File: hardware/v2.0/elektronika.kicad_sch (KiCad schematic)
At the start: 35 parts, among them J1 Conn_02x06_Odd_Even, J12 Conn_02x03_Counter_Clockwise, J2 Conn_01x06_Male, J3 Conn_01x06, Q4 Q_NMOS_GSD, Q5 Q_PMOS_GSD, Q6 Q_NMOS_GSD, Q7 Q_NMOS_GSD, Q8 Q_NMOS_GSD

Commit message: Secondary button cross
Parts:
- removed J12: Conn_02x03_Counter_Clockwise, Connector_PinSocket_2.54mm:PinSocket_2x03_P2.54mm_Vertical, symbol Connector_Generic:Conn_02x03_Counter_Clockwise
- added J12: Conn_01x02, Connector_PinSocket_2.54mm:PinSocket_1x02_P2.54mm_Vertical, symbol Connector_Generic:Conn_01x02
- added R32: 10k, Resistor_SMD:R_0402_1005Metric, symbol Device:R
- J1: footprint Connector_PinSocket_2.54mm:PinSocket_2x06_P2.54mm_Vertical -> Connector_PinSocket_2.54mm:PinSocket_2x06_P2.54mm_Horizontal
- J3: footprint Connector_PinSocket_2.54mm:PinSocket_1x06_P2.54mm_Vertical -> Connector_PinSocket_2.54mm:PinSocket_1x06_P2.54mm_Horizontal
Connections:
- net 3V3: now also R32.1; no longer Q7.1 (G), Q8.1 (G)
- net 5V: no longer R11.1, R18.1
- net ESP+programing/IO48: now also J12.1 (Pin_1)
- net GND: now also J12.2 (Pin_2)
- net IO15: now also J1.8 (Pin_8); no longer J1.2 (Pin_2)
- net IO16: now also J1.6 (Pin_6); no longer J1.4 (Pin_4)
- net IO17: now also J1.4 (Pin_4); no longer J1.6 (Pin_6)
- net IO18: now also J1.2 (Pin_2); no longer J1.8 (Pin_8)
- net IO35: now also J3.1 (Pin_1); no longer J1.1 (Pin_1)
- net IO36: now also J3.2 (Pin_2); no longer J1.3 (Pin_3)
- net IO37: now also J3.3 (Pin_3); no longer J1.5 (Pin_5)
- net IO38: now also J3.4 (Pin_4); no longer J1.7 (Pin_7)
- net IO39: now also J1.1 (Pin_1); no longer J3.1 (Pin_1)
- net IO40: now also J1.3 (Pin_3); no longer J3.2 (Pin_2)
- net IO41: now also J1.5 (Pin_5); no longer J3.3 (Pin_3)
- net IO42: now also J1.7 (Pin_7); no longer J3.4 (Pin_4)
- net SW_10: now also R10.2; no longer R12.2
- net SW_11: now also R9.2; no longer R14.2
- net SW_2: now also R6.2; no longer R1.2
- net SW_3: now also R7.2; no longer R4.2
- net SW_4: now also R12.2; no longer R6.2
- net SW_5: now also R4.2; no longer R7.2
- net SW_7: now also R1.2; no longer R8.2
- net SW_8: now also R8.2; no longer R9.2
- net SW_9: now also R14.2; no longer R10.2
- net VSTUP2: now also J2.4 (Pin_4); no longer J2.2 (Pin_2)
- net VSTUP3: now also J2.2 (Pin_2); no longer J2.4 (Pin_4)
- net V_LED_1: now also R11.1, R18.1
- new net EN: Q7.1 (G), Q8.1 (G)
- new net SW_12: R32.2
- no-connect marks 0 -> 1
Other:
- sheet ESP+programing ports: added EN; removed none

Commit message: SD karta and factory files
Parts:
- removed J2: Conn_01x06_Male, Connector_JST:JST_PH_S6B-PH-K_1x06_P2.00mm_Horizontal, symbol Connector:Conn_01x06_Male
- added C22, C23: 10uF, Capacitor_SMD:C_0603_1608Metric, symbol Device:C
- added J2: Micro_SD_Card, my_library:TF-01A, symbol Connector:Micro_SD_Card
- added R33, R34, R35, R36: 10k, Resistor_SMD:R_0402_1005Metric, symbol Device:R
- BZ1: LCSC ručně -> C3015481
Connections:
- net 3V3: now also C22.1, C23.1, J2.4 (VDD)
- net 5V: now also R33.2
- net ESP+programing/IO03-PD: now also J2.2 (DAT3/CD)
- net GND: now also C22.2, C23.2, J2.6 (VSS), J2.9 (SHIELD), R34.2, R35.2, R36.2
- net at BZ1.2 (+), D114.2 (A), Q6.3 (D): now also R33.1
- new net ESP+programing/IO11: J2.3 (CMD), R36.1
- new net ESP+programing/IO12: J2.5 (CLK), R35.1
- new net ESP+programing/IO13: J2.7 (DAT0), R34.1
- no-connect marks 1 -> 2
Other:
- moved on the sheet: D114, H3, H4

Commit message: RH v2 version
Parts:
- added J13: Conn_01x03, Connector_PinHeader_2.54mm:PinHeader_1x03_P2.54mm_Horizontal, symbol Connector_Generic:Conn_01x03
- BZ1: footprint my_library:PIEZO -> Robotarna_KiCad_Library:ELKS-PIEZO; LCSC C3015481 -> C201041
- J1: JLCPCB_CORRECTION (none) -> -1.27;6.35;270; LCSC (none) -> C2897426
- J12, J3: JLCPCB_IGNORE (none) -> 1
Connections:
- net 3V3: now also J13.1 (Pin_1)
- net 5V: now also J13.3 (Pin_3); no longer C1.1, C5.1, J1.11 (Pin_11), J1.12 (Pin_12)
- new net PMOD-POWER: C1.1, C5.1, J1.11 (Pin_11), J1.12 (Pin_12), J13.2 (Pin_2)
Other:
- note added: "používá ESP pullpu"
- note removed: "používá ESP pulldown"
- moved on the sheet: BZ1, D114, Q6, Q7, Q8, R11, R18, R19, R33

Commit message: Change piezo
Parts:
- BZ1: footprint Robotarna_KiCad_Library:ELKS-PIEZO -> Robotarna_KiCad_Library:PKLCS1212E-(RH-Logic_piezzo); LCSC C201041 -> C113159
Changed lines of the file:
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@@
     (property "Reference" "BZ1" (id 0) (at 58.42 125.73 0))
     (property "Value" "Buzzer" (id 1) (at 59.69 128.27 0))
-    (property "Footprint" "Robotarna_KiCad_Library:ELKS-PIEZO" (id 2) (at 59.055 130.81 90)
+    (property "Footprint" "Robotarna_KiCad_Library:PKLCS1212E-(RH-Logic_piezzo)" (id 2) (at 59.055 130.81 90)
       (effects (font (size 1.27 1.27)) hide)
     )
-    (property "Datasheet" "~" (id 3) (at 59.055 130.81 90)
+    (property "Datasheet" "https://datasheet.lcsc.com/lcsc/1808132343_Murata-Electronics-PKLCS1212E4001-R1_C113159.pdf" (id 3) (at 59.055 130.81 90)
       (effects (font (size 1.27 1.27)) hide)
     )
-    (property "LCSC" "C201041" (id 4) (at 59.69 133.35 0)
+    (property "LCSC" "C113159" (id 4) (at 59.69 133.35 0)
       (effects (font (size 1.27 1.27)) hide)
     )

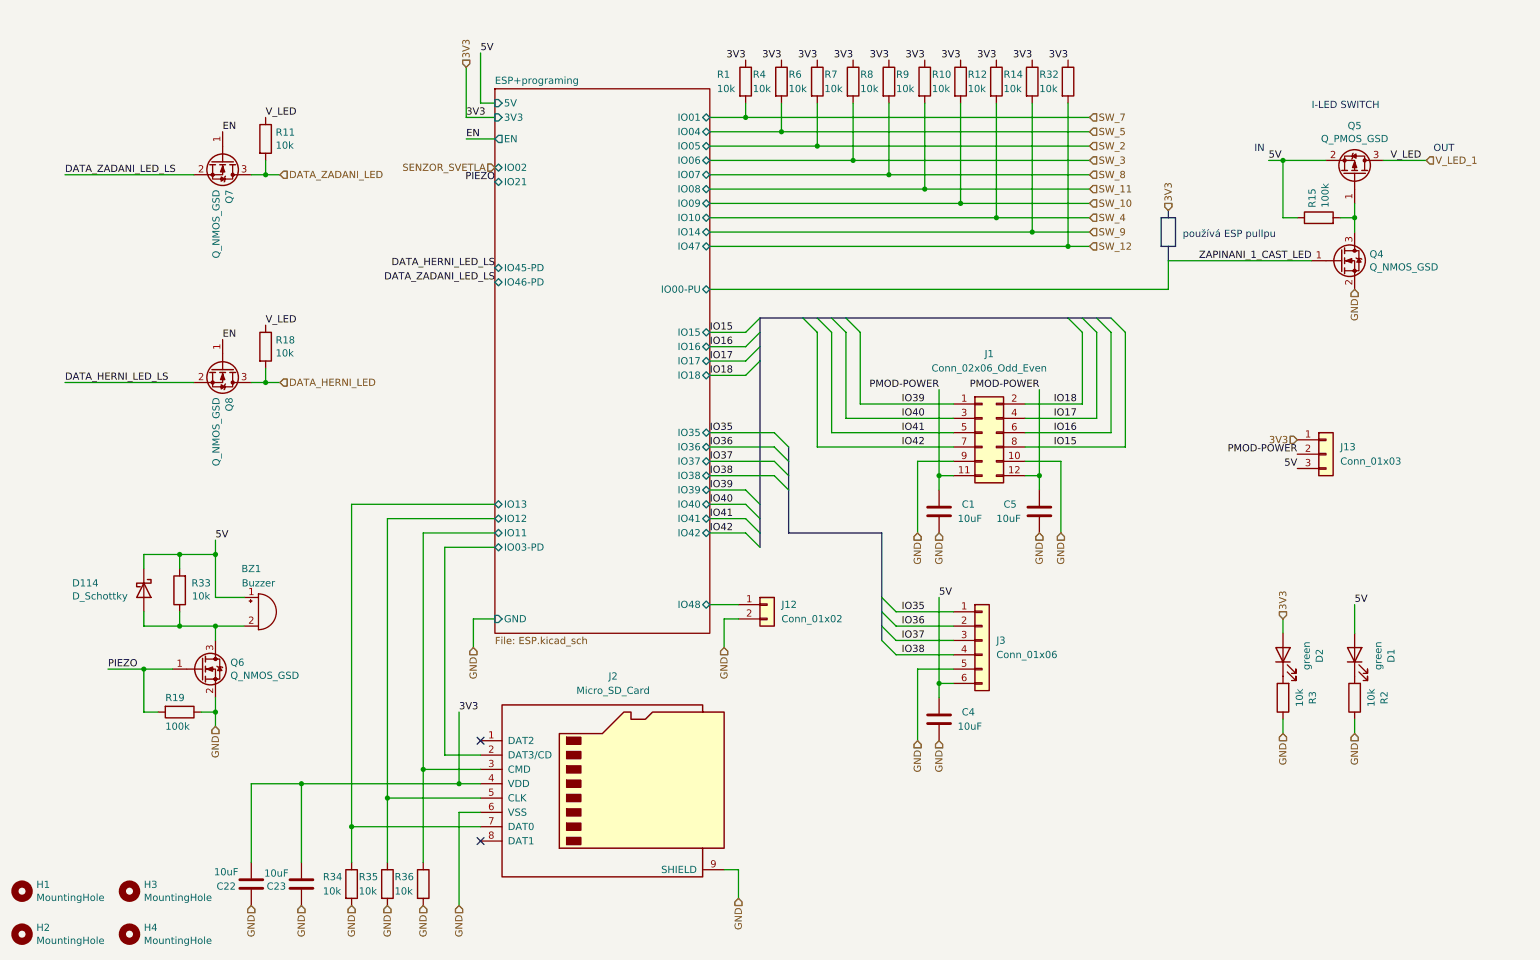
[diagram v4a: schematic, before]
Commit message: Microphone and a few minor changes
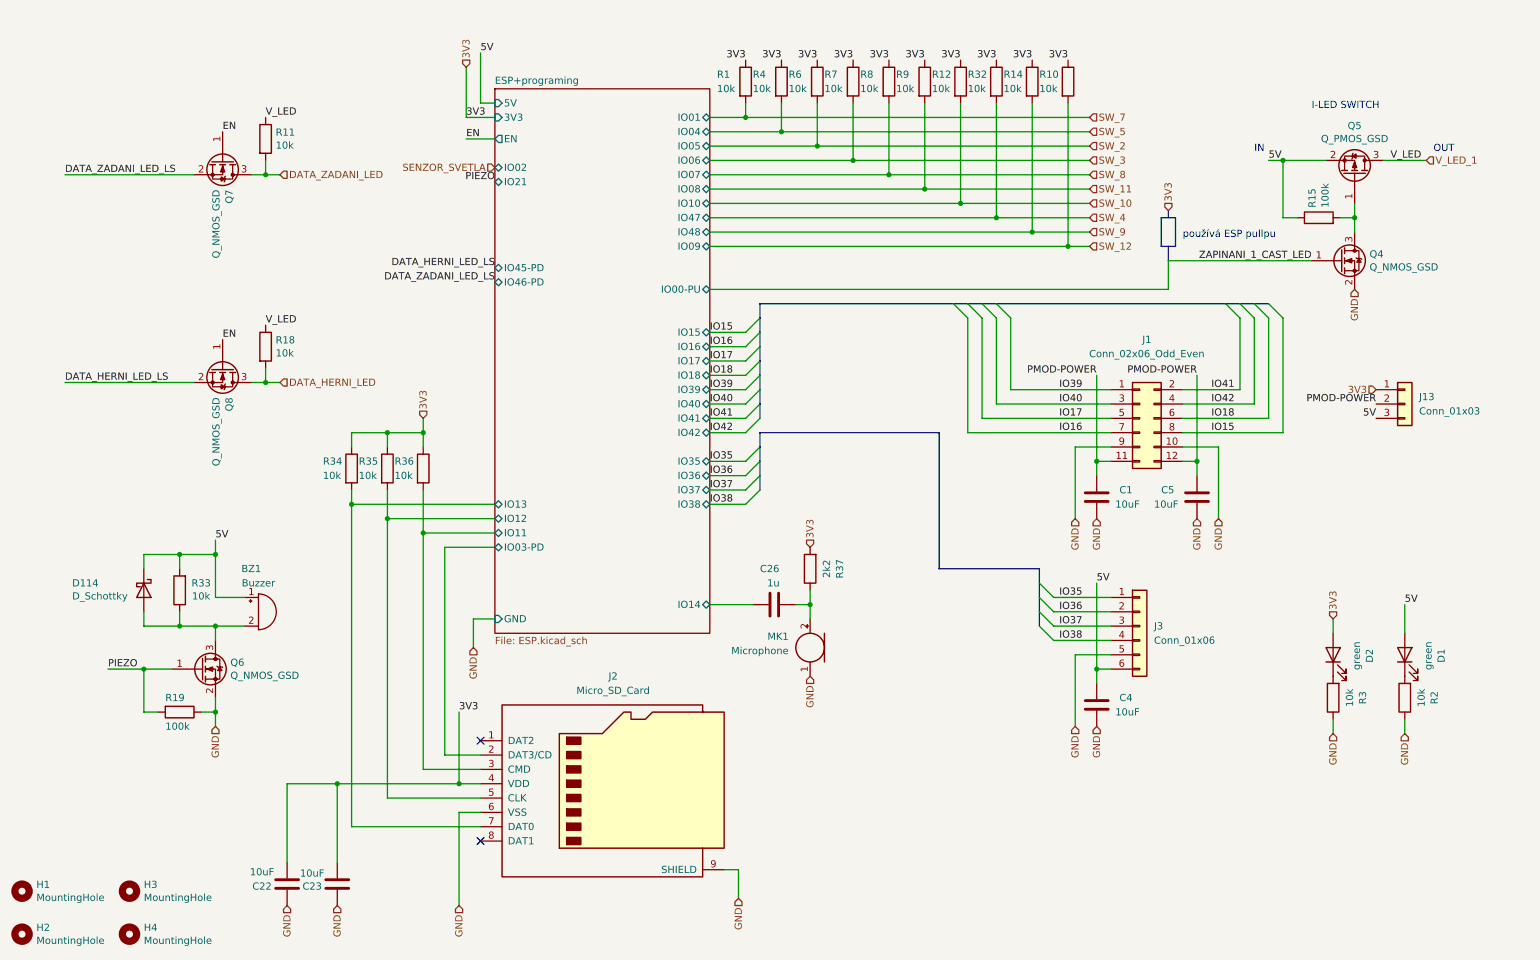
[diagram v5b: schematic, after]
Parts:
- removed J12: Conn_01x02, Connector_PinSocket_2.54mm:PinSocket_1x02_P2.54mm_Vertical, symbol Connector_Generic:Conn_01x02
- added C26: 1u, Capacitor_SMD:C_0402_1005Metric, symbol Device:C
- added MK1: Microphone, Robotarna_KiCad_Library:MIC-TH, symbol Device:Microphone
- added R37: 2k2, Resistor_SMD:R_0402_1005Metric, symbol Device:R
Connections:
- net 3V3: now also R34.1, R35.1, R36.1, R37.2
- net ESP+programing/IO11: now also R36.2; no longer R36.1
- net ESP+programing/IO12: now also R35.2; no longer R35.1
- net ESP+programing/IO13: now also R34.2; no longer R34.1
- net GND: now also MK1.1 (-); no longer R34.2, R35.2, R36.2
- net IO16: now also J1.7 (Pin_7); no longer J1.6 (Pin_6)
- net IO17: now also J1.5 (Pin_5); no longer J1.4 (Pin_4)
- net IO18: now also J1.6 (Pin_6); no longer J1.2 (Pin_2)
- net IO41: now also J1.2 (Pin_2); no longer J1.5 (Pin_5)
- net IO42: now also J1.4 (Pin_4); no longer J1.7 (Pin_7)
- net SW_10: now also R12.2; no longer R10.2
- net SW_12: now also R10.2; no longer R32.2
- net SW_4: now also R32.2; no longer R12.2
- new net: C26.2, MK1.2 (+), R37.1
- new net ESP+programing/IO14: C26.1
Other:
- moved on the sheet: C1, C22, C23, C4, C5, D1, D2, J1, J13, J3, R10, R12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

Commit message: Small tidy up
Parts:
- BZ1: footprint Robotarna_KiCad_Library:PKLCS1212E-(RH-Logic_piezzo) -> RKL-StandardPackages:PKLCS1212E-(RH-Logic_piezzo)
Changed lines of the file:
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@@
       (effects (font (size 1.27 1.27)))
     )
-    (property "Footprint" "Robotarna_KiCad_Library:PKLCS1212E-(RH-Logic_piezzo)" (at 59.055 130.81 90)
+    (property "Footprint" "RKL-StandardPackages:PKLCS1212E-(RH-Logic_piezzo)" (at 59.055 130.81 90)
       (effects (font (size 1.27 1.27)) hide)
     )

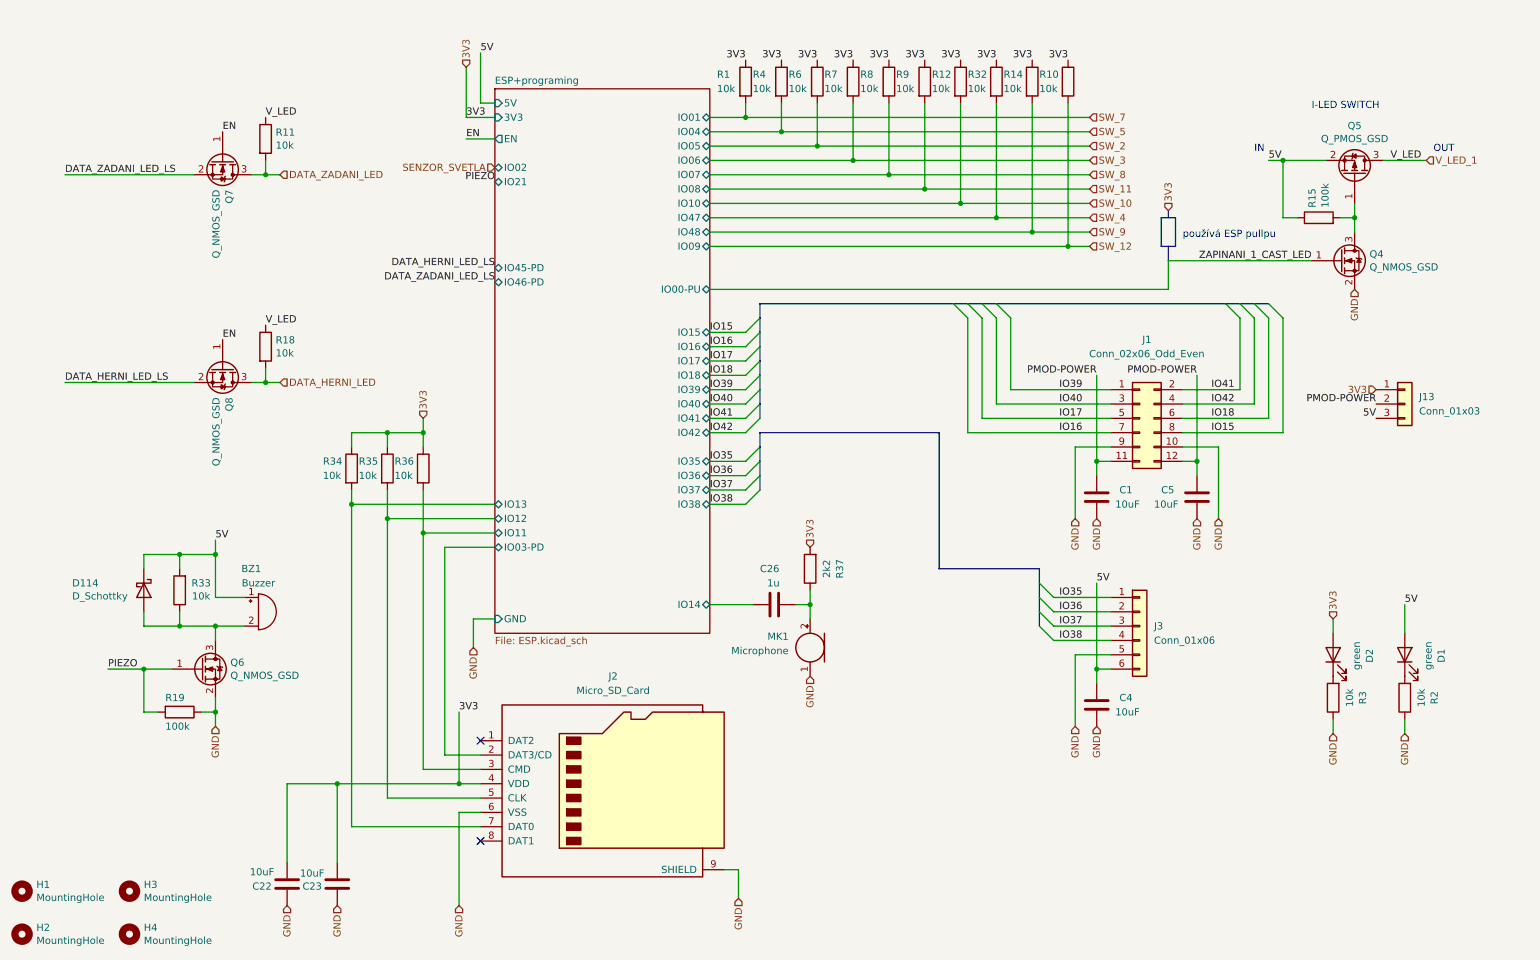
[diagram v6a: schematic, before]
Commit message: Fix PMOD conectors
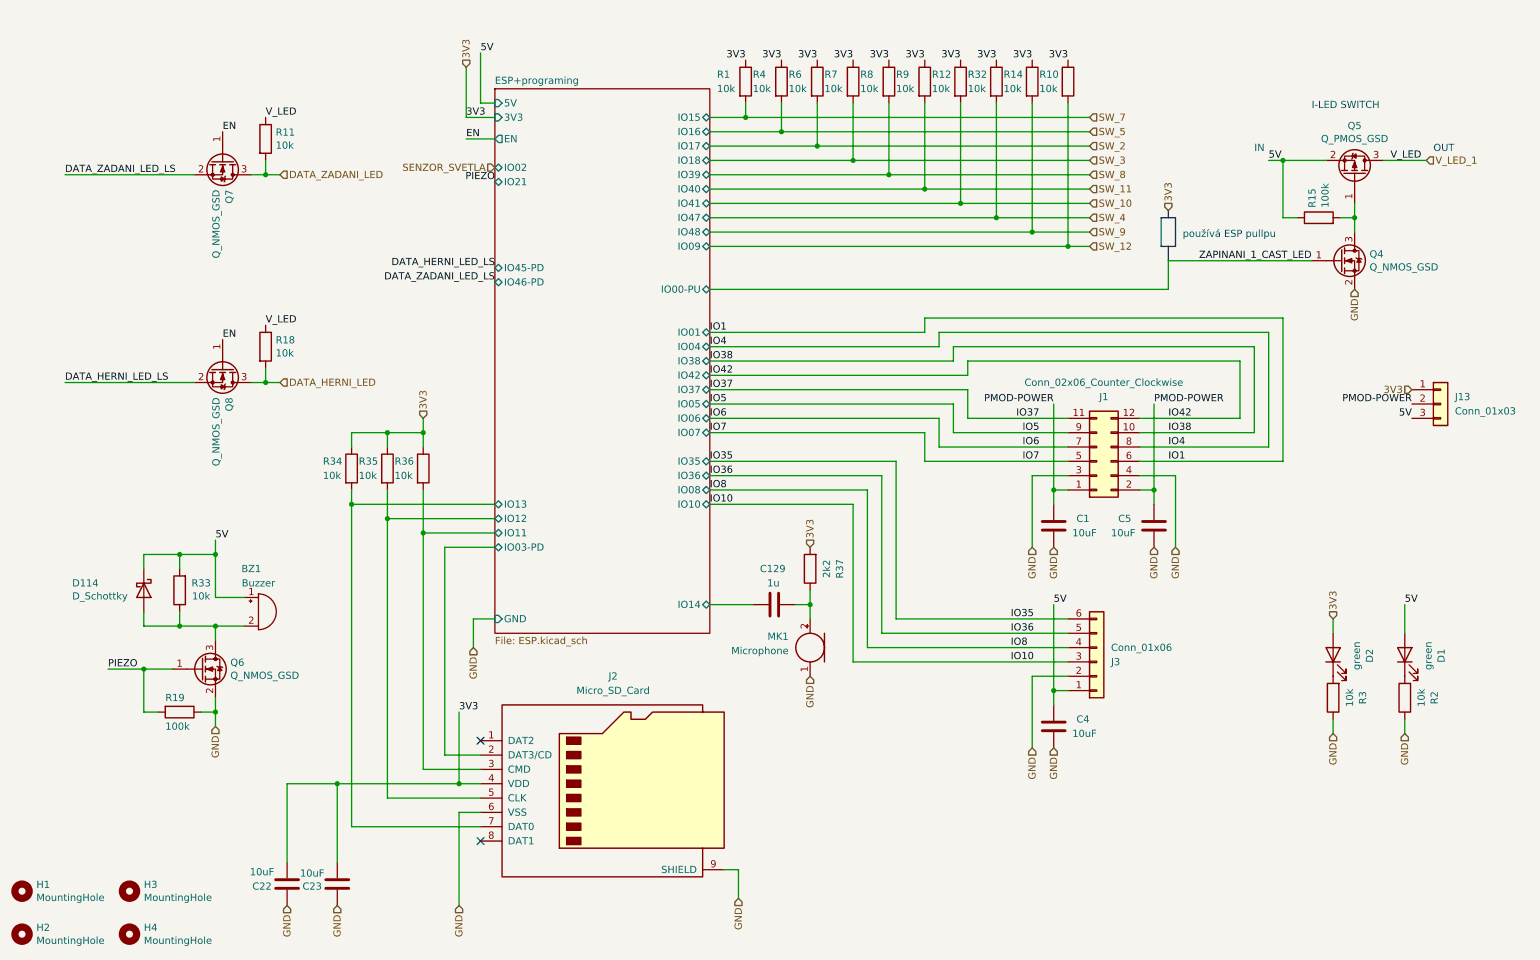
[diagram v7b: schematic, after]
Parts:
- J1: value Conn_02x06_Odd_Even -> Conn_02x06_Counter_Clockwise
- renumbered C26 to C129
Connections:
- net IO39 is gone; now on net PMOD-POWER: J1.1 (Pin_1)
- net IO40 is gone; now on net GND: J1.3 (Pin_3)
- net IO41 is gone; now on net PMOD-POWER: J1.2 (Pin_2)
- net 5V: now also J3.1 (Pin_1); no longer J3.6 (Pin_6)
- net GND: now also J1.4 (Pin_4), J3.2 (Pin_2); no longer J1.10 (Pin_10), J1.9 (Pin_9), J3.5 (Pin_5)
- net IO35: now also J3.6 (Pin_6); no longer J3.1 (Pin_1)
- net IO36: now also J3.5 (Pin_5); no longer J3.2 (Pin_2)
- net IO37: now also J1.11 (Pin_11); no longer J3.3 (Pin_3)
- net IO38: now also J1.10 (Pin_10); no longer J3.4 (Pin_4)
- net IO42: now also J1.12 (Pin_12); no longer J1.4 (Pin_4)
- net PMOD-POWER: no longer J1.11 (Pin_11), J1.12 (Pin_12)
- net IO15 renamed IO4
- net IO16 renamed IO6
- net IO17 renamed IO7
- net IO18 renamed IO1
- new net IO10: J3.3 (Pin_3)
- new net IO5: J1.9 (Pin_9)
- new net IO8: J3.4 (Pin_4)
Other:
- moved on the sheet: C1, C4, C5, J13, J3
